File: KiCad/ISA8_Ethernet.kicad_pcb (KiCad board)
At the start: 2 copper layers, 104.1 x 74.9 mm, 34 parts, among them J1 RJMG1BD3B8K1ANR, J2 MEM_EXT, SW1 CONFIG, SW2 IRQ, SW3 IO_ADDR, SW4 ROM_ADDR, U1 RTL8019AS, U2 SST39SF040, U3 93LC46C, Y1 20MHz

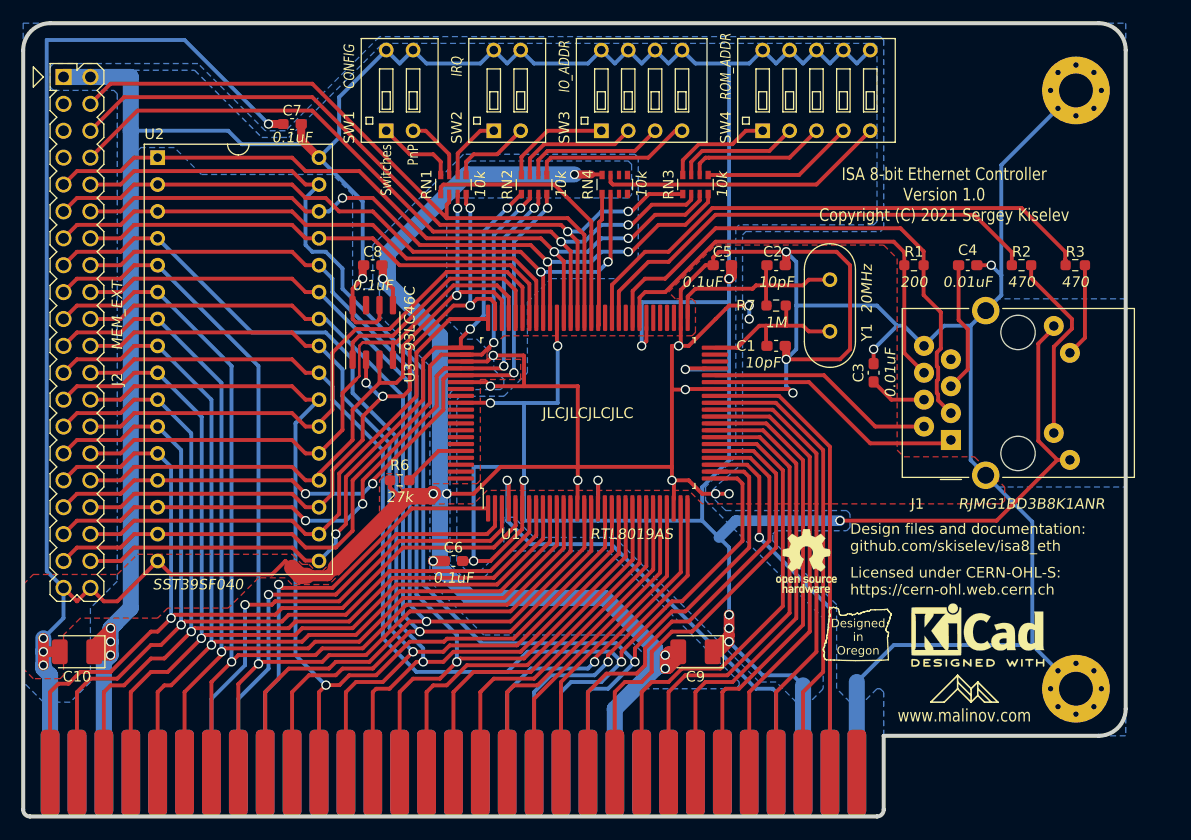
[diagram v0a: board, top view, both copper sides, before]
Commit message: modify board design for THT components
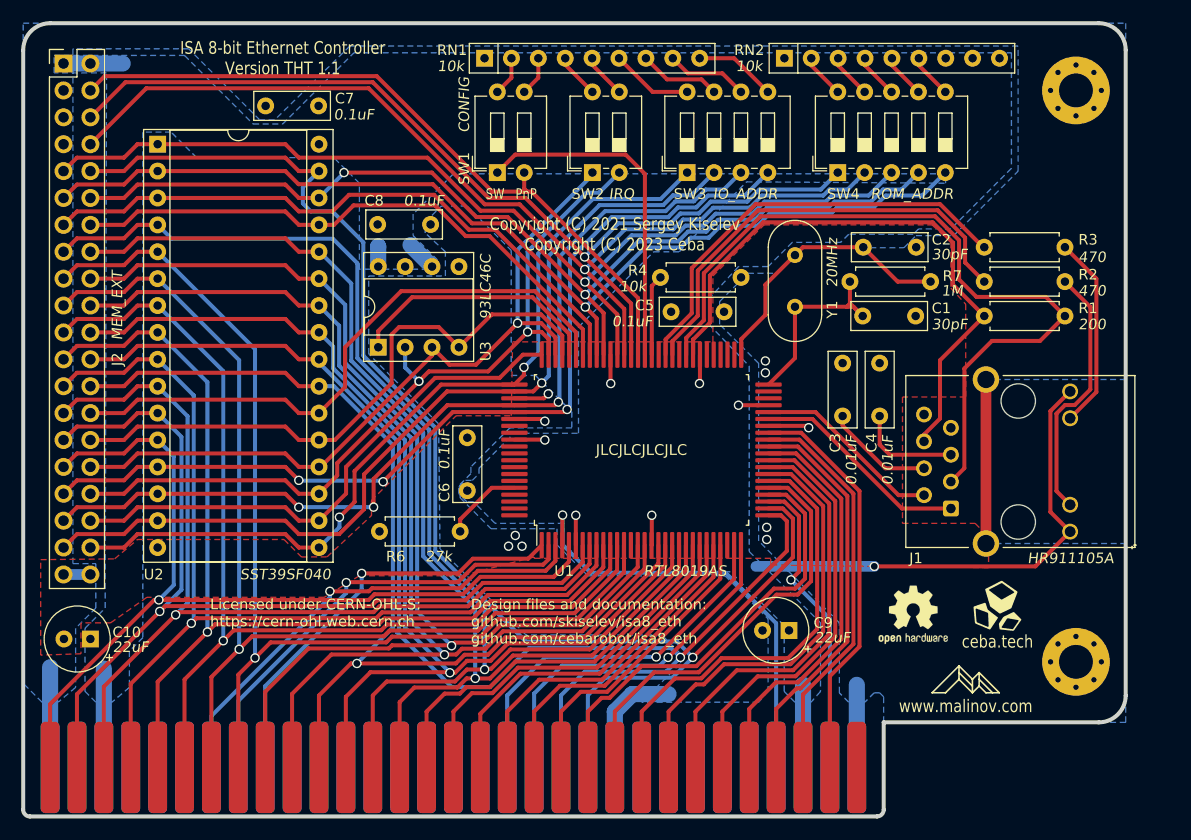
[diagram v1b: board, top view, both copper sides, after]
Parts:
- removed the REF** at (175.6, 110.5)
- removed the REF** at (191.8, 117.5)
- removed RN3, RN4: 10k, Resistor_SMD:R_Array_Convex_4x0603
- added R4: 10k, Resistor_THT:R_Axial_DIN0207_L6.3mm_D2.5mm_P7.62mm_Horizontal, F.Cu at (161.8, 83.7)
- added REF**: OSHW-Logo2_7.3x6mm_SilkScreen, Symbol:OSHW-Logo2_7.3x6mm_SilkScreen, F.Cu at (185.7, 115.6)
- C1, C2: value 10pF -> 30pF; footprint Capacitor_SMD:C_0603_1608Metric_Pad1.08x0.95mm_HandSolder -> Capacitor_THT:C_Disc_D7.0mm_W2.5mm_P5.00mm
- C10, C9: footprint Capacitor_Tantalum_SMD:CP_EIA-3528-15_AVX-H_Pad1.50x2.35mm_HandSolder -> Capacitor_THT:CP_Radial_Tantal_D6.0mm_P2.50mm
- C3, C4, C5, C6, C7, C8: footprint Capacitor_SMD:C_0603_1608Metric_Pad1.08x0.95mm_HandSolder -> Capacitor_THT:C_Disc_D7.0mm_W2.5mm_P5.00mm
- J1: value RJMG1BD3B8K1ANR -> HR911105A; footprint Connector_RJ:RJ45_Amphenol_RJMG1BD3B8K1ANR -> Connector_RJ:RJ45_Hanrun_HR911105A
- J2: footprint My_Components:Conn_Pin_Header_20x2_2.54mm -> Connector_PinHeader_2.54mm:PinHeader_2x20_P2.54mm_Vertical
- R1, R2, R3, R6, R7: footprint Resistor_SMD:R_0603_1608Metric_Pad0.98x0.95mm_HandSolder -> Resistor_THT:R_Axial_DIN0207_L6.3mm_D2.5mm_P7.62mm_Horizontal
- RN1, RN2: footprint Resistor_SMD:R_Array_Convex_4x0603 -> Resistor_THT:R_Array_SIP9
- SW1, SW2: footprint My_Components:Switch_DIP_2_Positions -> Button_Switch_THT:SW_DIP_SPSTx02_Slide_6.7x6.64mm_W7.62mm_P2.54mm_LowProfile
- SW3: footprint My_Components:Switch_DIP_4_Positions -> Button_Switch_THT:SW_DIP_SPSTx04_Slide_6.7x11.72mm_W7.62mm_P2.54mm_LowProfile
- SW4: footprint My_Components:Switch_DIP_5_Positions -> Button_Switch_THT:SW_DIP_SPSTx05_Slide_6.7x14.26mm_W7.62mm_P2.54mm_LowProfile
- U2: footprint My_Components:Socket_DIP32_600 -> Package_DIP:DIP-32_W15.24mm_Socket
- U3: footprint Package_SO:SO-8_3.9x4.9mm_P1.27mm -> Package_DIP:DIP-8_W7.62mm_Socket
- Y1: footprint My_Components:Crystal_HC-49U_Vert -> Crystal:Crystal_HC49-4H_Vertical
- moved RN2 26.5 mm to (173.5, 63.0), turned to 0 degrees
- moved J2 25.4 mm to (105.4, 63.5), turned to 0 degrees
- moved U2 21.7 mm to (114.3, 71.1), turned to 0 degrees
- moved C4 16.5 mm to (182.5, 96.8), turned to 90 degrees
- moved R1 15.0 mm to (200.0, 87.3)
- moved C1 13.5 mm to (185.9, 87.3)
- moved C2 13.3 mm to (185.9, 80.8)
- moved RN1 12.3 mm to (145.2, 63.0), turned to 0 degrees
- moved SW1 12.1 mm to (146.4, 73.8), turned to 90 degrees
- moved SW2 11.2 mm to (155.4, 73.8), turned to 90 degrees
- moved C9 9.06 mm to (173.9, 117.0)
- moved SW3 8.87 mm to (164.3, 73.8), turned to 90 degrees
- moved SW4 8.02 mm to (178.5, 73.8), turned to 90 degrees
- moved R7 7.33 mm to (179.7, 84.1), turned to 0 degrees
- moved C6 6.77 mm to (143.6, 103.8), turned to 90 degrees
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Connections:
- net /~BCS renamed /~{BCS}
- net /~IOCS16 renamed /~{IOCS16}
- net /~IOR renamed /~{IOR}
- net /~IOW renamed /~{IOW}
- net /~SMEMR renamed /~{SMEMR}
- net /~SMEMW renamed /~{SMEMW}
- BUS1 pad 15: Net-(BUS1-Pad15) -> unconnected-(BUS1-DACK3-Pad15)
- BUS1 pad 16: Net-(BUS1-Pad16) -> unconnected-(BUS1-DRQ3-Pad16)
- BUS1 pad 17: Net-(BUS1-Pad17) -> unconnected-(BUS1-DACK1-Pad17)
- BUS1 pad 18: Net-(BUS1-Pad18) -> unconnected-(BUS1-DRQ1-Pad18)
- BUS1 pad 19: Net-(BUS1-Pad19) -> unconnected-(BUS1-DACK0-Pad19)
- BUS1 pad 20: Net-(BUS1-Pad20) -> unconnected-(BUS1-CLK-Pad20)
- BUS1 pad 21: Net-(BUS1-Pad21) -> unconnected-(BUS1-IRQ7-Pad21)
- BUS1 pad 22: Net-(BUS1-Pad22) -> unconnected-(BUS1-IRQ6-Pad22)
- BUS1 pad 26: Net-(BUS1-Pad26) -> unconnected-(BUS1-DACK2-Pad26)
- BUS1 pad 27: Net-(BUS1-Pad27) -> unconnected-(BUS1-TC-Pad27)
- BUS1 pad 28: Net-(BUS1-Pad28) -> unconnected-(BUS1-ALE-Pad28)
- BUS1 pad 30: Net-(BUS1-Pad30) -> unconnected-(BUS1-OSC-Pad30)
- BUS1 pad 32: Net-(BUS1-Pad32) -> unconnected-(BUS1-IO_CH_CK-Pad32)
- BUS1 pad 5: Net-(BUS1-Pad5) -> unconnected-(BUS1--5V-Pad5)
- BUS1 pad 6: Net-(BUS1-Pad6) -> unconnected-(BUS1-DRQ2-Pad6)
- BUS1 pad 7: Net-(BUS1-Pad7) -> unconnected-(BUS1--12V-Pad7)
- BUS1 pad 8: Net-(BUS1-Pad8) -> unconnected-(BUS1-UNUSED-Pad8)
- BUS1 pad 9: Net-(BUS1-Pad9) -> unconnected-(BUS1-+12V-Pad9)
- C3 pad 1: Net-(C3-Pad1) -> Net-(J1-TCT)
- C4 pad 1: Net-(C4-Pad1) -> Net-(J1-RCT)
- J2 pad 3: Net-(J2-Pad3) -> unconnected-(J2-Pin_3-Pad3)
- J2 pad 5: Net-(J2-Pad5) -> unconnected-(J2-Pin_5-Pad5)
- J2 pad 7: Net-(J2-Pad7) -> unconnected-(J2-Pin_7-Pad7)
- R2 pad 1: Net-(J1-PadL3) -> Net-(J1-LEDG_K)
- R3 pad 1: Net-(J1-PadL2) -> Net-(J1-LEDY_K)
- RN1 pad 1: /JP -> VCC
- RN1 pad 2: /BA21 -> Net-(RN1-R1)
- RN1 pad 3: /BD6 -> Net-(RN1-R2)
- RN1 pad 4: /BD5 -> Net-(RN1-R3)
- RN1 pad 5: Net-(RN1-Pad5) -> Net-(RN1-R4)
- RN1 pad 6: Net-(RN1-Pad6) -> Net-(RN1-R5)
- RN1 pad 7: Net-(RN1-Pad7) -> Net-(RN1-R6)
- RN1 pad 8: Net-(RN1-Pad8) -> Net-(RN1-R7)
- RN2 pad 1: /BD3 -> VCC
- RN2 pad 2: /BD2 -> Net-(RN2-R1)
- RN2 pad 3: /BD1 -> Net-(RN2-R2)
- RN2 pad 4: /BD0 -> Net-(RN2-R3)
- RN2 pad 5: Net-(RN2-Pad5) -> Net-(RN2-R4)
- RN2 pad 6: Net-(RN2-Pad6) -> Net-(RN2-R5)
- RN2 pad 7: Net-(RN2-Pad7) -> unconnected-(RN2-R6-Pad7)
- RN2 pad 8: Net-(RN2-Pad8) -> unconnected-(RN2-R7-Pad8)
- SW1 pad 1: Net-(RN1-Pad8) -> /JP
- SW1 pad 2: Net-(RN1-Pad7) -> /BA21
- SW1 pad 3: VCC -> Net-(RN1-R2)
- SW1 pad 4: VCC -> Net-(RN1-R1)
- SW2 pad 1: Net-(RN1-Pad6) -> /BD6
- SW2 pad 2: Net-(RN1-Pad5) -> /BD5
- SW2 pad 3: VCC -> Net-(RN1-R4)
- SW2 pad 4: VCC -> Net-(RN1-R3)
- SW3 pad 1: Net-(RN2-Pad8) -> /BD3
- SW3 pad 2: Net-(RN2-Pad7) -> /BD2
- SW3 pad 3: Net-(RN2-Pad6) -> /BD1
- SW3 pad 4: Net-(RN2-Pad5) -> /BD0
- SW3 pad 5: VCC -> Net-(RN1-R8)
- SW3 pad 6: VCC -> Net-(RN1-R7)
- SW3 pad 7: VCC -> Net-(RN1-R6)
- SW3 pad 8: VCC -> Net-(RN1-R5)
- SW4 pad 1: Net-(RN3-Pad8) -> /BA20
- SW4 pad 10: VCC -> Net-(RN2-R1)
- SW4 pad 2: Net-(RN3-Pad7) -> /BA19
- SW4 pad 3: Net-(RN3-Pad6) -> /BA18
- SW4 pad 4: Net-(RN3-Pad5) -> /BA17
- SW4 pad 5: Net-(RN4-Pad7) -> /BA16
- SW4 pad 6: VCC -> Net-(RN2-R5)
- SW4 pad 7: VCC -> Net-(RN2-R4)
- SW4 pad 8: VCC -> Net-(RN2-R3)
- SW4 pad 9: VCC -> Net-(RN2-R2)
- U1 pad 100: Net-(U1-Pad100) -> unconnected-(U1-INT4/IRQ10-Pad100)
- U1 pad 48: Net-(U1-Pad48) -> unconnected-(U1-TX--Pad48)
- U1 pad 49: Net-(U1-Pad49) -> unconnected-(U1-TX+-Pad49)
- U1 pad 53: Net-(U1-Pad53) -> unconnected-(U1-CD--Pad53)
- U1 pad 54: Net-(U1-Pad54) -> unconnected-(U1-CD+-Pad54)
- U1 pad 55: Net-(U1-Pad55) -> unconnected-(U1-RX--Pad55)
- U1 pad 56: Net-(U1-Pad56) -> unconnected-(U1-RX+-Pad56)
- U1 pad 60: Net-(U1-Pad60) -> unconnected-(U1-LEDBNC-Pad60)
- U1 pad 63: Net-(U1-Pad63) -> unconnected-(U1-LED2/LED_TX-Pad63)
- U1 pad 87: Net-(U1-Pad87) -> unconnected-(U1-SD15-Pad87)
- U1 pad 88: Net-(U1-Pad88) -> unconnected-(U1-SD14-Pad88)
- U1 pad 90: Net-(U1-Pad90) -> unconnected-(U1-SD13-Pad90)
- U1 pad 91: Net-(U1-Pad91) -> unconnected-(U1-SD12-Pad91)
- U1 pad 92: Net-(U1-Pad92) -> unconnected-(U1-SD11-Pad92)
- U1 pad 93: Net-(U1-Pad93) -> unconnected-(U1-SD10-Pad93)
- U1 pad 94: Net-(U1-Pad94) -> unconnected-(U1-SD9-Pad94)
- U1 pad 95: Net-(U1-Pad95) -> unconnected-(U1-SD8-Pad95)
- U1 pad 97: Net-(U1-Pad97) -> unconnected-(U1-INT7/IRQ15-Pad97)
- U1 pad 98: Net-(U1-Pad98) -> unconnected-(U1-INT6/IRQ12-Pad98)
- U1 pad 99: Net-(U1-Pad99) -> unconnected-(U1-INT5/IRQ11-Pad99)
- U3 pad 7: Net-(U3-Pad7) -> unconnected-(U3-NC-Pad7)
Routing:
- net GND: track 538.4 -> 58.3 mm, vias 26 -> 10
- net VCC: track 426.0 -> 90.4 mm, vias 16 -> 7
- net /BA16: track 68.1 -> 99.9 mm, vias 2 -> 1
- net Net-(RN4-Pad7): track 27.4 -> 0.00 mm
- net Net-(J1-LEDG_K): track 0.00 -> 24.5 mm
- net /BA17: track 71.8 -> 96.2 mm, vias 3 -> 2
- net /TP_RX+: track 51.0 -> 73.6 mm
- net /BA18: track 74.9 -> 97.1 mm, vias 2 -> 1
- net /BA19: track 74.3 -> 95.8 mm, vias 2 -> 1
- net /BA20: track 73.4 -> 93.2 mm, vias 2 -> 1
- net /BD0: track 69.0 -> 88.4 mm, vias 4 -> 3
- net Net-(J1-LEDY_K): track 0.00 -> 18.4 mm
- net /BD1: track 69.8 -> 88.2 mm, vias 4 -> 3
- net Net-(J1-PadL3): track 18.2 -> 0.00 mm
- net Net-(RN2-Pad5): track 15.2 -> 0.00 mm
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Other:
- outline, holes or cut-outs redrawn
- net class Default removed
- net class Power removed
- board text added: "Copyright (C) 2021 Sergey Kiselev Copyright (C) 2023 Ceba"
- board text added: "Design files and documentation: github.com/skiselev/isa8_eth github.com/cebarobot/isa8_eth"
- board text added: "I/O Addr 0x200 0x220 0x240 0x260 0x280 0x2A0 0x2C0 0x2E0"
- board text added: "I/O Addr 0x300 0x320 0x340 0x360 0x380 0x3A0 0x3C0 0x3E0"
- board text added: "ISA 8-bit Ethernet Controller Version THT 1.1"
- board text added: "ROM Addr Boot ROM Disabled 0xC0000 0xC4000 0xC8000 0xCC000 0xD0000 0xD4000 0xD8000 0xDC000 0xC0000 0xC8000 0xD0000 0xD8000 0xC0000 0xD0000"
- board text added: "SW"
- board text added: "ceba.tech"
- board text added: "~{CS}"
- board text added: "~{MEMR}"
- board text added: "~{MEMW}"
- board text removed: "Design files and documentation: github.com/skiselev/isa8_eth"
- board text removed: "Designed in Oregon"
- board text removed: "I/O Address 0x200 0x220 0x240 0x260 0x280 0x2A0 0x2C0 0x2E0"
- board text removed: "I/O Address 0x300 0x320 0x340 0x360 0x380 0x3A0 0x3C0 0x3E0"
- board text removed: "ISA 8-bit Ethernet Controller Version 1.0 Copyright (C) 2021 Sergey Kiselev"
- board text removed: "ROM Address Boot ROM Disabled 0xC0000 0xC4000 0xC8000 0xCC000 0xD0000 0xD4000 0xD8000 0xDC000 0xC0000 0xC8000 0xD0000 0xD8000 0xC0000 0xD0000"
- board text removed: "Switches"
- board text removed: "~CS"
- board text removed: "~MEMR"
- board text removed: "~MEMW"
